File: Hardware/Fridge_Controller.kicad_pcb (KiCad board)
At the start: 2 copper layers, 91 x 67 mm, 0 parts

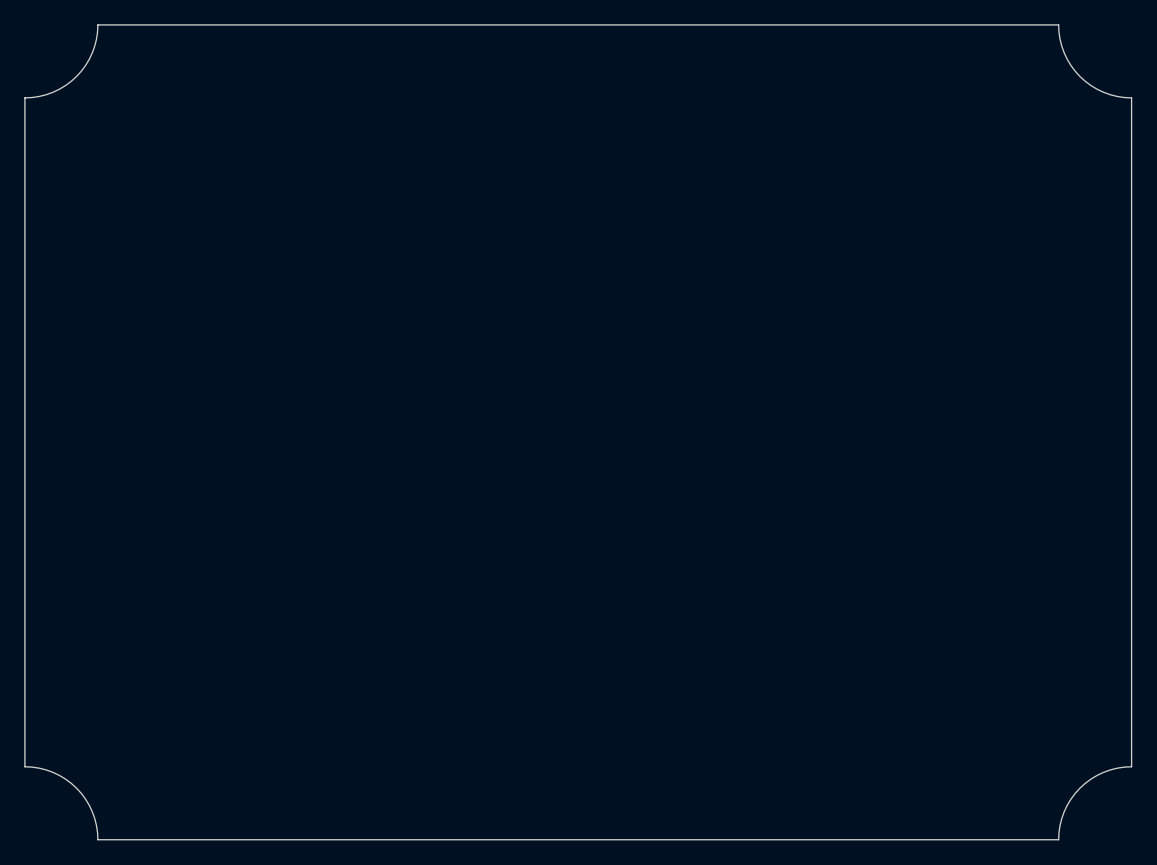
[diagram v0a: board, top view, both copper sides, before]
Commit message: [Hardware] Placed components on the PCB, added the logic ground planes and the keepout areas for the mains voltage.
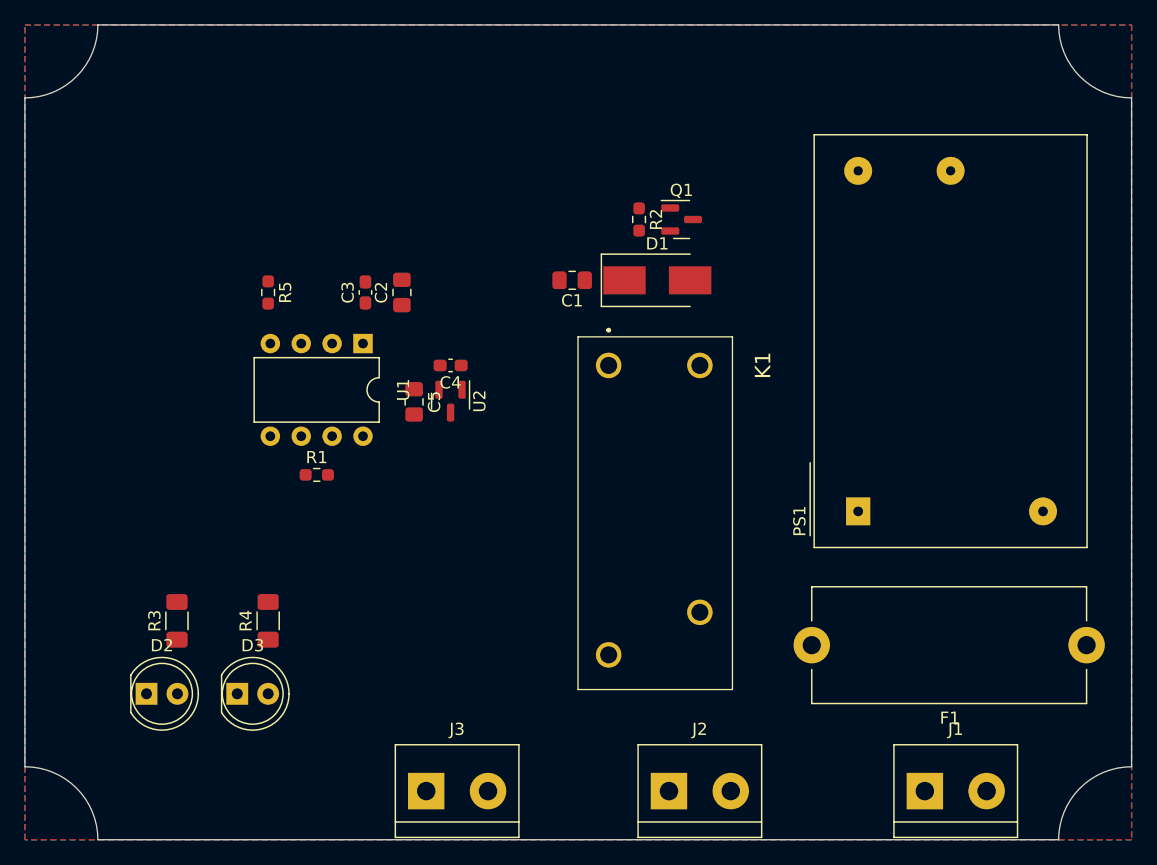
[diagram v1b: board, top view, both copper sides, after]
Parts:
- added C1: 2.2u, Capacitor_SMD:C_0805_2012Metric_Pad1.18x1.45mm_HandSolder, F.Cu at (145.0, 94.0)
- added C2: 2.2u, Capacitor_SMD:C_0805_2012Metric_Pad1.18x1.45mm_HandSolder, F.Cu at (131.0, 95.0)
- added C3: 100n, Capacitor_SMD:C_0603_1608Metric_Pad1.08x0.95mm_HandSolder, F.Cu at (128.0, 95.0)
- added C4: 100n, Capacitor_SMD:C_0603_1608Metric_Pad1.08x0.95mm_HandSolder, F.Cu at (135.0, 101.0)
- added C5: 2.2u, Capacitor_SMD:C_0805_2012Metric_Pad1.18x1.45mm_HandSolder, F.Cu at (132.0, 104.0)
- added D1: S1BB-13-F, Diode_SMD:D_SMB_Handsoldering, F.Cu at (152.0, 94.0)
- added D2: Power, LED_THT:LED_D5.0mm, F.Cu at (110.0, 128.0)
- added D3: Compressor, LED_THT:LED_D5.0mm, F.Cu at (117.5, 128.0)
- added F1: 696101000002, Fuse:Fuseholder_Cylinder-5x20mm_Stelvio-Kontek_PTF78_Horizontal_Open, F.Cu at (187.3, 124.0)
- added J1: CTB0508/2, TerminalBlock:TerminalBlock_bornier-2_P5.08mm, F.Cu at (174.0, 136.0)
- added J2: CTB0508/2, TerminalBlock:TerminalBlock_bornier-2_P5.08mm, F.Cu at (153.0, 136.0)
- added J3: CTB0508/2, TerminalBlock:TerminalBlock_bornier-2_P5.08mm, F.Cu at (133.0, 136.0)
- added K1: RZ01-1A4-D005, RZ01-1A4-D005:RZ01-1A4-D005, F.Cu at (148.0, 101.0)
- added PS1: IRM-02-5, Converter_ACDC:Converter_ACDC_MeanWell_IRM-02-xx_THT, F.Cu at (168.5, 113.0)
- added Q1: DMG3414U, Package_TO_SOT_SMD:SOT-23, F.Cu at (154.0, 89.0)
- added R1: 10K, Resistor_SMD:R_0603_1608Metric_Pad0.98x0.95mm_HandSolder, F.Cu at (124.0, 110.0)
- added R2: 10K, Resistor_SMD:R_0603_1608Metric_Pad0.98x0.95mm_HandSolder, F.Cu at (150.5, 89.0)
- added R3: 270, Resistor_SMD:R_1206_3216Metric_Pad1.30x1.75mm_HandSolder, F.Cu at (112.5, 122.0)
- added R4: 270, Resistor_SMD:R_1206_3216Metric_Pad1.30x1.75mm_HandSolder, F.Cu at (120.0, 122.0)
- added R5: 10K, Resistor_SMD:R_0603_1608Metric_Pad0.98x0.95mm_HandSolder, F.Cu at (120.0, 95.0)
- added U1: PIC12F683-IP, Package_DIP:DIP-8_W7.62mm, F.Cu at (127.8, 99.2)
- added U2: MCP1541T-ITT, Package_TO_SOT_SMD:SOT-23, F.Cu at (135.0, 103.9)
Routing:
- added copper zone on B.Cu, net GND
- added copper zone on F.Cu, net GND

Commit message: [Hardware] Routed all PCB tracks.
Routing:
- net +5V: track 0.00 -> 170.5 mm
- net Net-(Q1-Pad1): track 0.00 -> 37.9 mm, vias 0 -> 1
- net Net-(J3-Pad2): track 0.00 -> 34.8 mm
- net Net-(R4-Pad2): track 0.00 -> 32.3 mm, vias 0 -> 1
- net Net-(J2-Pad2): track 0.00 -> 31.5 mm
- net Net-(J2-Pad1): track 0.00 -> 30.0 mm
- net Net-(J1-Pad1): track 0.00 -> 25.3 mm
- net Net-(F1-Pad2): track 0.00 -> 23.6 mm
- net Net-(R3-Pad2): track 0.00 -> 16.8 mm
- net Net-(F1-Pad1): track 0.00 -> 16.8 mm
- net +4V: track 0.00 -> 15.8 mm
- net Net-(D1-Pad2): track 0.00 -> 12.4 mm
- net Net-(D2-Pad2): track 0.00 -> 4.47 mm
- net Net-(D3-Pad2): track 0.00 -> 4.45 mm
- net Net-(R5-Pad2): track 0.00 -> 3.36 mm
- added copper zone on F.Cu, net +4V
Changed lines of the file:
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@@
   )
   (setup
+    (stackup
+      (layer "F.SilkS" (type "Top Silk Screen"))
+      (layer "F.Paste" (type "Top Solder Paste"))
+      (layer "F.Mask" (type "Top Solder Mask") (thickness 0.01))
+      (layer "F.Cu" (type "copper") (thickness 0.035))
+      (layer "dielectric 1" (type "core") (thickness 1.51) (material "FR4") (epsilon_r 4.5) (loss_tangent 0.02))
+      (layer "B.Cu" (type "copper") (thickness 0.035))
+      (layer "B.Mask" (type "Bottom Solder Mask") (thickness 0.01))
+      (layer "B.Paste" (type "Bottom Solder Paste"))
+      (layer "B.SilkS" (type "Bottom Silk Screen"))
+      (copper_finish "None")
+      (dielectric_constraints no)
+    )
     (pad_to_mask_clearance 0)
     (aux_axis_origin 100.000001 139.999999)
@@
     (style (thickness 0.1) (arrow_length 1.27) (text_position_mode 0) (extension_height 0.58642) (extension_offset 0.5) keep_text_aligned)
   )
+  (segment (start 127.8 96.2) (end 128 96) (width 1.6) (layer "F.Cu") (net 1))
+  (segment (start 149.3 94) (end 149.3 99.7) (width 2) (layer "F.Cu") (net 1))
+  (segment (start 135.8625 101) (end 135.8625 99.2125) (width 0.6) (layer "F.Cu") (net 1))
+  (segment (start 135.95 101.0875) (end 135.8625 101) (width 0.6) (layer "F.Cu") (net 1))
+  (segment (start 131 96.0375) (end 128.175 96.0375) (width 1.6) (layer "F.Cu") (net 1))
+  (segment (start 149.3 99.7) (end 148 101) (width 2) (layer "F.Cu") (net 1))
+  (segment (start 127.8 99.2) (end 127.8 96.2) (width 1.6) (layer "F.Cu") (net 1))
+  (segment (start 148 104) (end 149 105) (width 2) (layer "F.Cu") (net 1))
+  (segment (start 131 96.0375) (end 139.0375 96.0375) (width 1.6) (layer "F.Cu") (net 1))
+  (segment (start 159 105) (end 176.1175 87.8825) (width 2) (layer "F.Cu") (net 1))
+  (segment (start 124 95) (end 125 96) (width 1) (layer "F.Cu") (net 1))
+  (segment (start 125 96) (end 127.8625 96) (width 1) (layer "F.Cu") (net 1))
+  (segment (start 139.0375 96.0375) (end 144 101) (width 1.6) (layer "F.Cu") (net 1))
+  (segment (start 148 101) (end 148 104) (width 2) (layer "F.Cu") (net 1))
+  (segment (start 120 94.0875) (end 120 82) (width 2) (layer "F.Cu") (net 1))
+  (segment (start 176.1175 85) (end 176.1175 81.1175) (width 2) (layer "F.Cu") (net 1))
+  (segment (start 135.95 103) (end 135.95 101.0875) (width 0.6) (layer "F.Cu") (net 1))
+  (segment (start 144 101) (end 148 101) (width 1.6) (layer "F.Cu") (net 1))
+  (segment (start 174 79) (end 123 79) (width 2) (layer "F.Cu") (net 1))
+  (segment (start 176.1175 87.8825) (end 176.1175 85) (width 2) (layer "F.Cu") (net 1))
+  (segment (start 127.8625 96) (end 128 95.8625) (width 1) (layer "F.Cu") (net 1))
+  (segment (start 159 105) (end 149 105) (width 2) (layer "F.Cu") (net 1))
+  (segment (start 128.175 96.0375) (end 128 95.8625) (width 1.6) (layer "F.Cu") (net 1))
+  (segment (start 120 94.0875) (end 123.0875 94.0875) (width 1) (layer "F.Cu") (net 1))
+  (segment (start 123.0875 94.0875) (end 124 95) (width 1) (layer "F.Cu") (net 1))
+  (segment (start 176.1175 81.1175) (end 174 79) (width 2) (layer "F.Cu") (net 1))
+  (segment (start 146.0375 94) (end 149.3 94) (width 1.6) (layer "F.Cu") (net 1))
+  (segment (start 123 79) (end 122 80) (width 2) (layer "F.Cu") (net 1))
+  (segment (start 120 82) (end 123 79) (width 2) (layer "F.Cu") (net 1))
+  (segment (start 135.8625 99.2125) (end 139.0375 96.0375) (width 0.6) (layer "F.Cu") (net 1))
+  (segment (start 122.72 104.28) (end 122.72 106.82) (width 1) (layer "F.Cu") (net 3))
+  (segment (start 122.72 106.82) (end 122.72 109.6325) (width 1) (layer "F.Cu") (net 3))
+  (segment (start 124.0375 102.9625) (end 122.72 104.28) (width 1) (layer "F.Cu") (net 3))
+  (segment (start 132 102.9625) (end 124.0375 102.9625) (width 1) (layer "F.Cu") (net 3))
+  (segment (start 122.72 109.6325) (end 123.0875 110) (width 1) (layer "F.Cu") (net 3))
+  (segment (start 132.0375 103) (end 132 102.9625) (width 1) (layer "F.Cu") (net 3))
+  (segment (start 154.7 89.2375) (end 154.9375 89) (width 1) (layer "F.Cu") (net 4))
+  (segment (start 154.7 100.2) (end 155.5 101) (width 2) (layer "F.Cu") (net 4))
+  (segment (start 154.7 94) (end 154.7 100.2) (width 2) (layer "F.Cu") (net 4))
+  (segment (start 154.7 94) (end 154.7 89.2375) (width 1) (layer "F.Cu") (net 4))
+  (segment (start 112.5 127.96) (end 112.54 128) (width 1) (layer "F.Cu") (net 5))
+  (segment (start 112.5 123.55) (end 112.5 127.96) (width 1) (layer "F.Cu") (net 5))
+  (segment (start 120 123.55) (end 120 128) (width 1) (layer "F.Cu") (net 6))
+  (segment (start 185 124) (end 179.08 129.92) (width 3.2) (layer "F.Cu") (net 7))
+  (segment (start 179.08 129.92) (end 179.08 136) (width 3.2) (layer "F.Cu") (net 7))
+  (segment (start 187.3 124) (end 185 124) (width 3.2) (layer "F.Cu") (net 7))
+  (segment (start 172.7175 124) (end 183.7175 113) (width 3.2) (layer "B.Cu") (net 8))
+  (segment (start 164.7 124) (end 172.7175 124) (width 3.2) (layer "B.Cu") (net 8))
+  (segment (start 174 136) (end 174 118.4825) (width 3.2) (layer "F.Cu") (net 9))
+  (segment (start 174 118.4825) (end 168.5175 113) (width 3.2) (layer "F.Cu") (net 9))
+  (segment (start 150 136) (end 148 134) (width 3.2) (layer "F.Cu") (net 10))
+  (segment (start 148 134) (end 148 124.8) (width 3.2) (layer "F.Cu") (net 10))
+  (segment (start 152.96 136) (end 150 136) (width 3.2) (layer "F.Cu") (net 10))
+  (segment (start 148 124.8) (end 148 134) (width 3.2) (layer "B.Cu") (net 10))
+  (segment (start 148 134) (end 150 136) (width 3.2) (layer "B.Cu") (net 10))
+  (segment (start 150 136) (end 152.96 136) (width 3.2) (layer "B.Cu") (net 10))
+  (segment (start 158.04 130.04) (end 158.04 136) (width 3.2) (layer "F.Cu") (net 11))
+  (segment (start 155.5 127.5) (end 158.04 130.04) (width 3.2) (layer "F.Cu") (net 11))
+  (segment (start 155.5 121.3) (end 155.5 127.5) (width 3.2) (layer "F.Cu") (net 11))
+  (segment (start 155.5 127.5) (end 158.04 130.04) (width 3.2) (layer "B.Cu") (net 11))
+  (segment (start 155.5 121.3) (end 155.5 127.5) (width 3.2) (layer "B.Cu") (net 11))
+  (segment (start 158.04 130.04) (end 158.04 136) (width 3.2) (layer "B.Cu") (net 11))
+  (segment (start 125.26 106.82) (end 125.26 109.6525) (width 1) (layer "F.Cu") (net 12))
+  (segment (start 125.26 109.6525) (end 124.9125 110) (width 1) (layer "F.Cu") (net 12))
+  (segment (start 124.9125 114.9125) (end 138.08 128.08) (width 1) (layer "F.Cu") (net 12))
+  (segment (start 138.08 128.08) (end 138.08 136) (width 1) (layer "F.Cu") (net 12))
+  (segment (start 124.9125 110) (end 124.9125 114.9125) (width 1) (layer "F.Cu") (net 12))
+  (segment (start 153.025 88.0875) (end 153.0625 88.05) (width 0.6) (layer "F.Cu") (net 13))
+  (segment (start 148 88) (end 150.4125 88) (width 0.6) (layer "F.Cu") (net 13))
+  (segment (start 150.5 88.0875) (end 153.025 88.0875) (width 0.6) (layer "F.Cu") (net 13))
+  (segment (start 150.4125 88) (end 150.5 88.0875) (width 0.6) (layer "F.Cu") (net 13))
+  (via (at 148 88) (size 0.8) (drill 0.4) (layers "F.Cu" "B.Cu") (net 13))
+  (segment (start 122.72 94.28) (end 129 88) (width 1) (layer "B.Cu") (net 13))
+  (segment (start 129 88) (end 148 88) (width 1) (layer "B.Cu") (net 13))
+  (segment (start 122.72 99.2) (end 122.72 94.28) (width 1) (layer "B.Cu") (net 13))
+  (segment (start 120.18 106.82) (end 120.18 109.82) (width 1) (layer "F.Cu") (net 14))
+  (segment (start 120.18 109.82) (end 112.5 117.5) (width 1) (layer "F.Cu") (net 14))
+  (segment (start 112.5 117.5) (end 112.5 120.45) (width 1) (layer "F.Cu") (net 14))
+  (segment (start 120 118) (end 120 120.45) (width 1) (layer "F.Cu") (net 15))
+  (via (at 120 118) (size 0.8) (drill 0.4) (layers "F.Cu" "B.Cu") (net 15))
+  (segment (start 131 105) (end 131 108) (width 1) (layer "B.Cu") (net 15))
+  (segment (start 125.26 101.26) (end 127 103) (width 1) (layer "B.Cu") (net 15))
+  (segment (start 131 111) (end 128 114) (width 1) (layer "B.Cu") (net 15))
+  (segment (start 131 108) (end 131 111) (width 1) (layer "B.Cu") (net 15))
+  (segment (start 121 116) (end 120 117) (width 1) (layer "B.Cu") (net 15))
+  (segment (start 128 114) (end 126 116) (width 1) (layer "B.Cu") (net 15))
+  (segment (start 127 103) (end 128 104) (width 1) (layer "B.Cu") (net 15))
+  (segment (start 125.26 99.2) (end 125.26 101.26) (width 1) (layer "B.Cu") (net 15))
+  (segment (start 126 116) (end 121 116) (width 1) (layer "B.Cu") (net 15))
+  (segment (start 128 104) (end 130 104) (width 1) (layer "B.Cu") (net 15))
+  (segment (start 120 117) (end 120 118) (width 1) (layer "B.Cu") (net 15))
+  (segment (start 130 104) (end 131 105) (width 1) (layer "B.Cu") (net 15))
+  (segment (start 120 95.9125) (end 120 99.02) (width 1) (layer "F.Cu") (net 16))
+  (segment (start 120 99.02) (end 120.18 99.2) (width 1) (layer "F.Cu") (net 16))
+  (zone (net 3) (net_name "+4V") (layer "F.Cu") (hatch edge 0.508)
+    (priority 2)
+    (connect_pads yes (clearance 0))
+    (min_thickness 0.254) (filled_areas_thickness no)
+    (fill yes (thermal_gap 0.508) (thermal_bridge_width 0.508))
+    (polygon
+      (pts
+        (xy 134.35 103.75)
+        (xy 131.35 103.75)
+        (xy 131.35 102.25)
+        (xy 134.35 102.25)
+      )
+    )
+  )
   (zone (net 2) (net_name "GND") (layers F&B.Cu) (hatch edge 0.508)
     (connect_pads (clearance 0.508))
@@
     (connect_pads (clearance 0))
     (min_thickness 0.254)
-    (keepout (tracks not_allowed) (vias not_allowed) (pads not_allowed) (copperpour not_allowed) (footprints allowed))
+    (keepout (tracks allowed) (vias allowed) (pads allowed) (copperpour not_allowed) (footprints allowed))
     (fill (thermal_gap 0.508) (thermal_bridge_width 0.508))
     (polygon
